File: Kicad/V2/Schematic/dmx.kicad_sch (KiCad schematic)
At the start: 12 parts, among them J5 XLR5_Ground, U7 B0505S-1W1, U8 6N137, U9 MAX485E

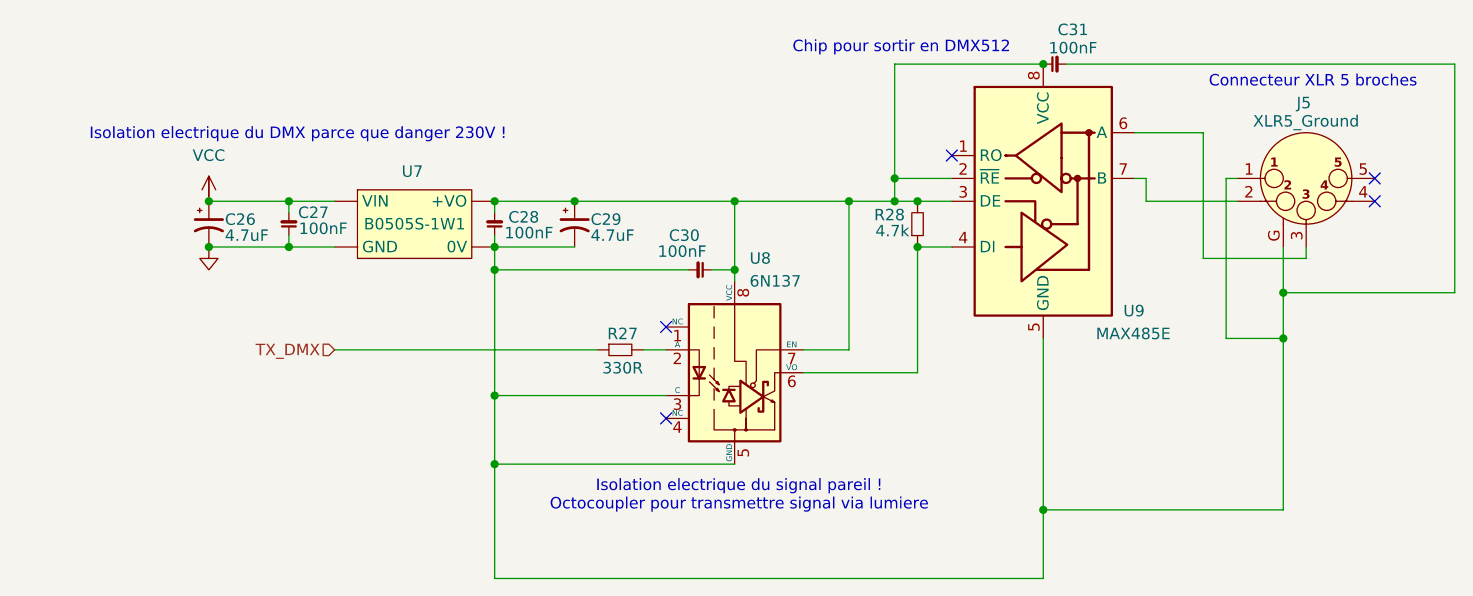
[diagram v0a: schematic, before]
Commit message: Split power and data
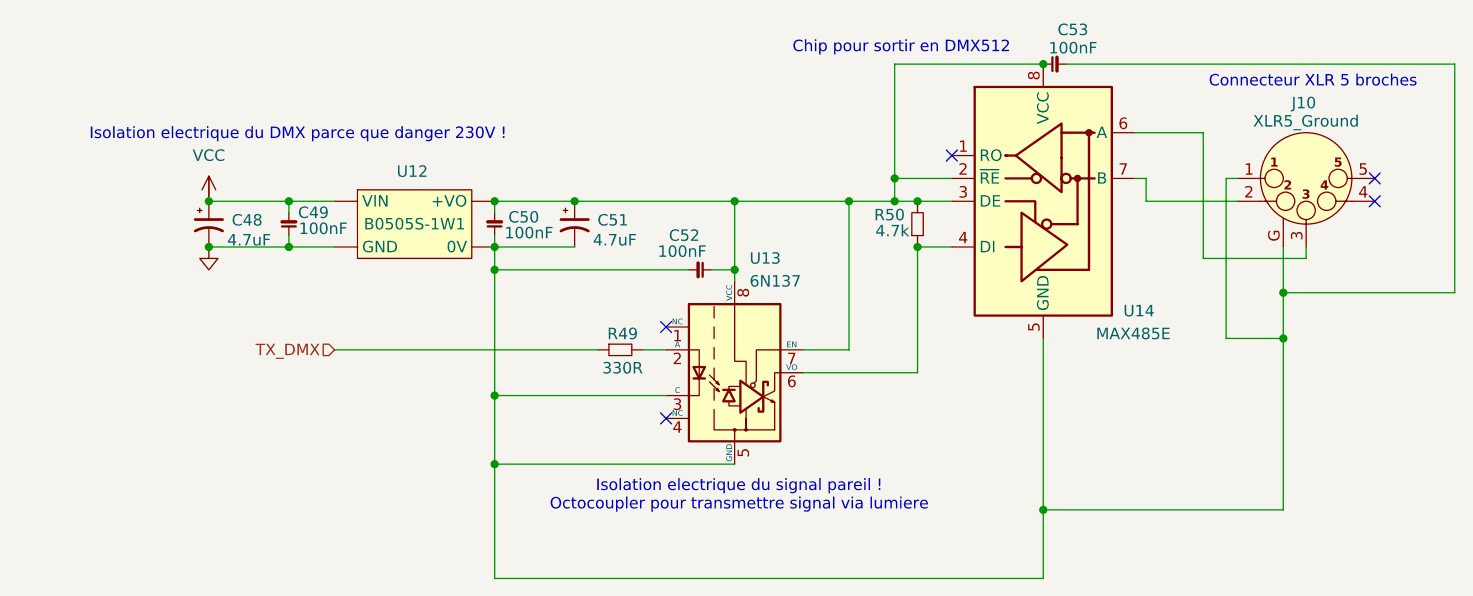
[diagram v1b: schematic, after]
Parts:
- removed C26, C29: 4.7uF, MyGlove:Capacitor_Electrolytic, symbol Device:C_Polarized_Small_US
- added C48, C51: 4.7uF, MyGlove:Capacitor_Electrolytic, symbol G-Love:C_Electrolytic
- renumbered C27 to C49, C28 to C50, C30 to C52, C31 to C53, J5 to J10, R27 to R49, R28 to R50, U7 to U12, U8 to U13, U9 to U14
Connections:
- net GND: now also C48.2
- net VCC: now also C48.1
- net at C50.2, C52.1, C53.1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: now also C51.2
- net at C50.1, C52.2, C53.2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: now also C51.1
